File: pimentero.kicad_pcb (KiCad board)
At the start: 2 copper layers, 20.8 x 11.3 mm, 12 parts, among them J1 Conn_01x04_Female, Q1 MMBF5457

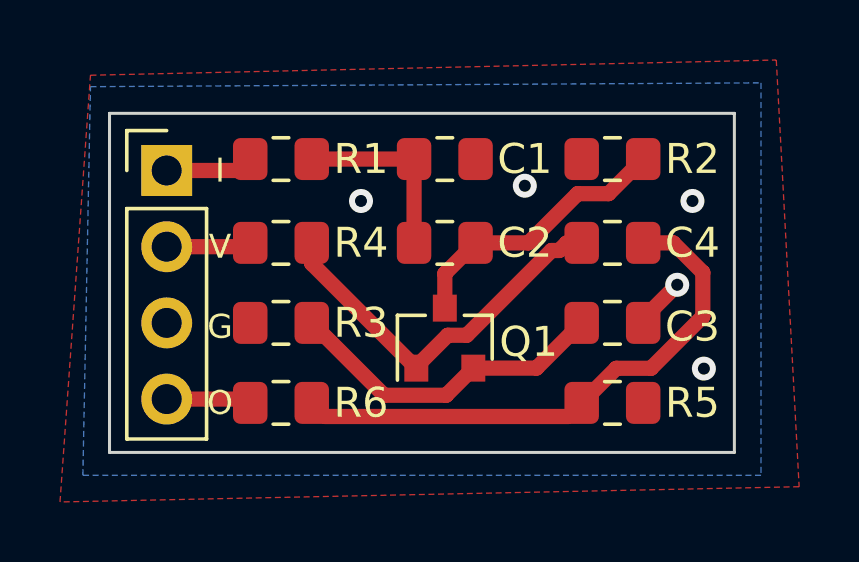
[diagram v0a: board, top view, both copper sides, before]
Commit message: v0.2: added volume pot (only pad for lug 1; lug 2 = GND, lug 3 = NC)
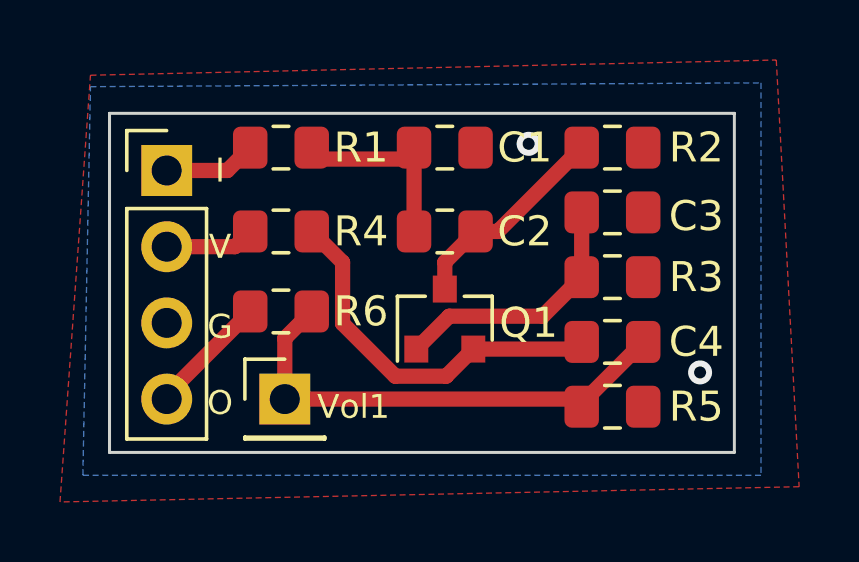
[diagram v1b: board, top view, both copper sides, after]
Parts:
- added J2: Volume A500k lug 1, Connector_PinHeader_2.54mm:PinHeader_1x01_P2.54mm_Vertical, F.Cu at (108.8, 75.9)
- moved R3 11.2 mm to (119.8, 71.9), turned to 0 degrees
- moved C3 3.68 mm to (119.8, 69.7)
- moved C4 3.30 mm to (119.8, 74.0)
- moved R6 3.05 mm to (108.7, 73.0)
- moved Q1 0.64 mm to (114.2, 73.3)
- moved C1 0.38 mm to (114.2, 67.6)
- moved C2 0.38 mm to (114.2, 70.4)
- moved R1 0.38 mm to (108.7, 67.6)
- moved R2 0.38 mm to (119.8, 67.6), turned to 0 degrees
- moved R4 0.38 mm to (108.7, 70.4)
- moved R5 0.13 mm to (119.8, 76.2)
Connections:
- Q1 pad 1: Net-(C4-Pad1) -> Net-(C3-Pad1)
- Q1 pad 2: Net-(C3-Pad1) -> Net-(C4-Pad1)
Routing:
- net Net-(C3-Pad1): track 11.0 -> 8.66 mm
- net Net-(C2-Pad2): track 9.34 -> 7.04 mm
- net Net-(C4-Pad2): track 18.5 -> 16.5 mm
- net GND: track 1.74 -> 0.00 mm, vias 5 -> 2
- net OUT: track 2.84 -> 4.07 mm
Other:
- board text added: "Vol1"
